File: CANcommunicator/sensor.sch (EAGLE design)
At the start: 19 parts, among them Y1 32.768kHz

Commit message: CAN sensor data ingestion
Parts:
- removed C11, C12: 560pF, SparkFun-Capacitors:560PF-0603-50V-5%
- removed R7: 4.7k, SparkFun-Resistors:4.7KOHM-0603-1/10W-1%
- added ACCEL: 22-23-2051, con-molex:22-23-2051
- added ADC, CAN0: 22-23-2021, con-molex:22-23-2021
- added CC2, CC3: 560pF, SparkFun-Capacitors:560PF-0603-50V-5%
- added CR1: 4.7k, SparkFun-Resistors:4.7KOHM-0603-1/10W-1%
- added IR1: 330, SparkFun-Resistors:330OHM-0603-1/10W-1%
- added PROGRAM: CORTEX_DEBUG_PTH, SparkFun-Connectors:CORTEX_DEBUG_PTH
- added SENSOR: 22-23-2031, con-molex:22-23-2031
- added SERCOM0, SERCOM1: 22-23-2041, con-molex:22-23-2041
- added STATUS: GREEN, SparkFun-LED:LED3MM
- renumbered C1 to PC2, C13 to CC1, C2 to PC1, C3 to IC2, C4 to IC3, C5 to IC1, C6 to OC1, C7 to OC2, R8 to CR3, R9 to CR2, U$1 to MCU, Y1 to O1
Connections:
- net N$1 renamed VDDANA
- net N$2 renamed VDDCORE
- net N$3 renamed XIN32
- net N$5 renamed XOUT32
- removed net 5V: CANI1.VSS, CC1.2
- removed net N$12: CANI1.RS, R7.1
- removed net N$13: C11.1, CR2.1
- removed net N$14: C12.1, CR3.1
- new net A0: ADC-1.S, MCU.PA02(AIN0)
- new net A1: ADC-2.S, MCU.PA03(AIN1)
- new net A4: MCU.PA04(AIN4), SENSOR-2.S
- new net A5: ACCEL-3.S, MCU.PA05(AIN5)
- new net A6: ACCEL-4.S, MCU.PA06(AIN6)
- new net A7: ACCEL-5.S, MCU.PA07(AIN7)
- new net C1HRC: CC2.1, CR2.1
- new net C1LRC: CC3.1, CR3.1
- new net C1RS: CANI1.RS, CR1.1
- new net LEDA: MCU.PA28, STATUS.A
- new net LEDC: IR1.2, STATUS.C
- new net RESET: MCU./RESET, PROGRAM.!RESET
- new net S00: MCU.PA08(SER00), SERCOM0-1.S
- new net S01: MCU.PA09(SER01), SERCOM0-2.S
- new net S02: MCU.PA10(SER02), SERCOM0-3.S
- new net S03: MCU.PA11(SER03), SERCOM0-4.S
- new net S10: MCU.PA16(SER10), SERCOM1-1.S
- new net S11: MCU.PA17(SER11), SERCOM1-2.S
- new net S12: MCU.PA18(SER12), SERCOM1-3.S
- new net S13: MCU.PA19(SER13), SERCOM1-4.S
- new net SWDCLK: MCU.PA30(SWCLK), PROGRAM.SWDCLK/TCK
- new net SWDIO: MCU.PA31(SWDIO), PROGRAM.SWDIO/TMS
- net CAN1H: now also CAN0-1.S
- net CAN1L: now also CAN0-2.S
- net CAN1RX: now also MCU.PA25(CANRX)
- net CAN1TX: now also MCU.PA24(CANTX)
- net GND: now also ACCEL-2.S, CC2.2, CC3.2, CR1.2, IR1.1, PROGRAM.GND@3, PROGRAM.GND@5, PROGRAM.GNDDTCT, SENSOR-3.S; no longer C11.2, C12.2, R7.2
- net VCC: now also ACCEL-1.S, CANI1.VSS, CC1.2, PROGRAM.VCC, SENSOR-1.S
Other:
- note added: "1"
- note added: "CAN Sensor Data Ingestion"
- note added: "EL-05154-AA"
- moved on the sheet: PWR-1, PWR-2

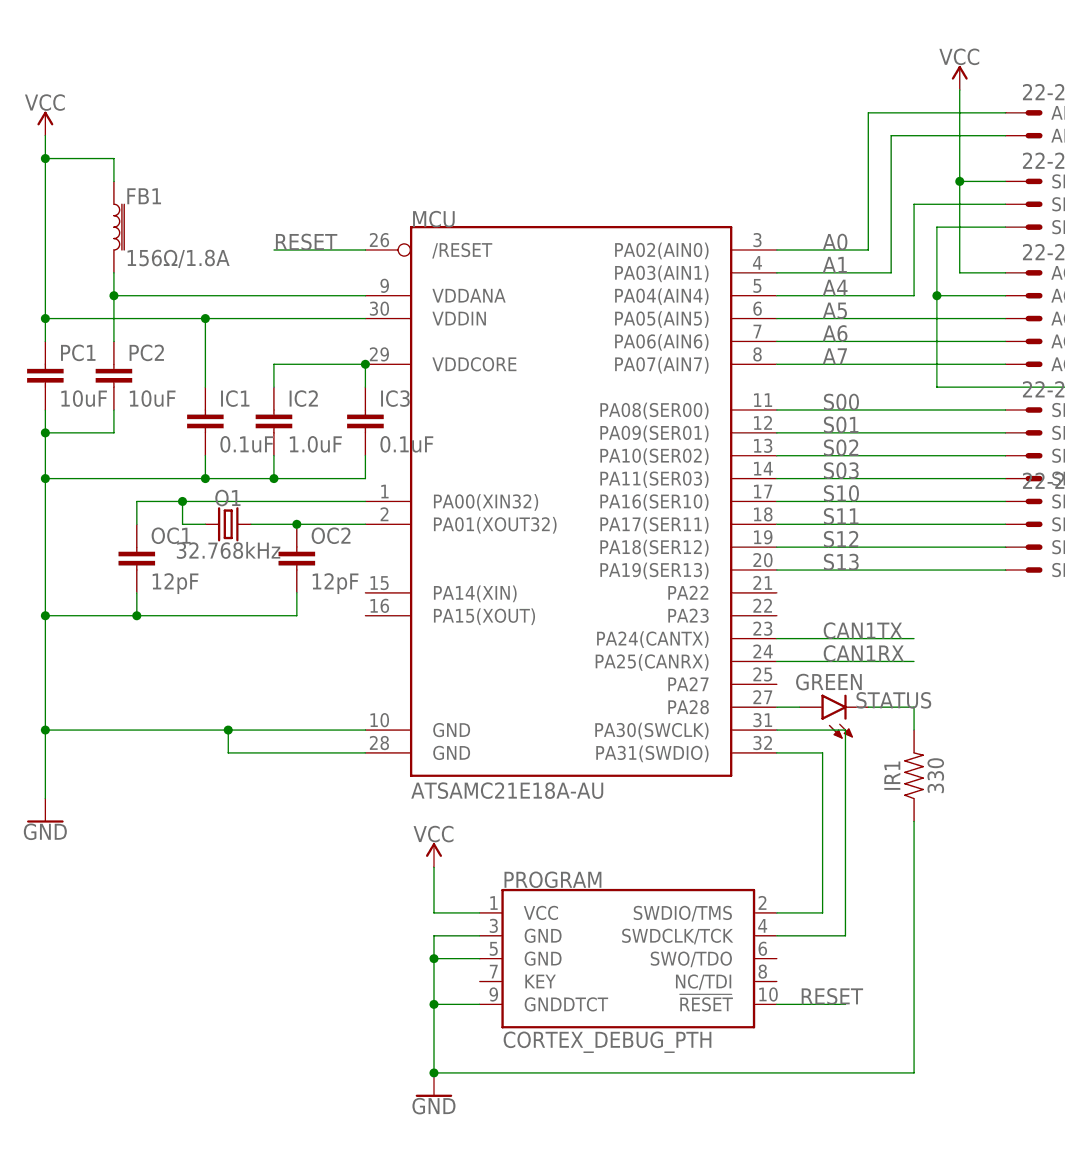
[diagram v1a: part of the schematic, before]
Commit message: Add pullup on SWDCLK and RC filter on RESET_L
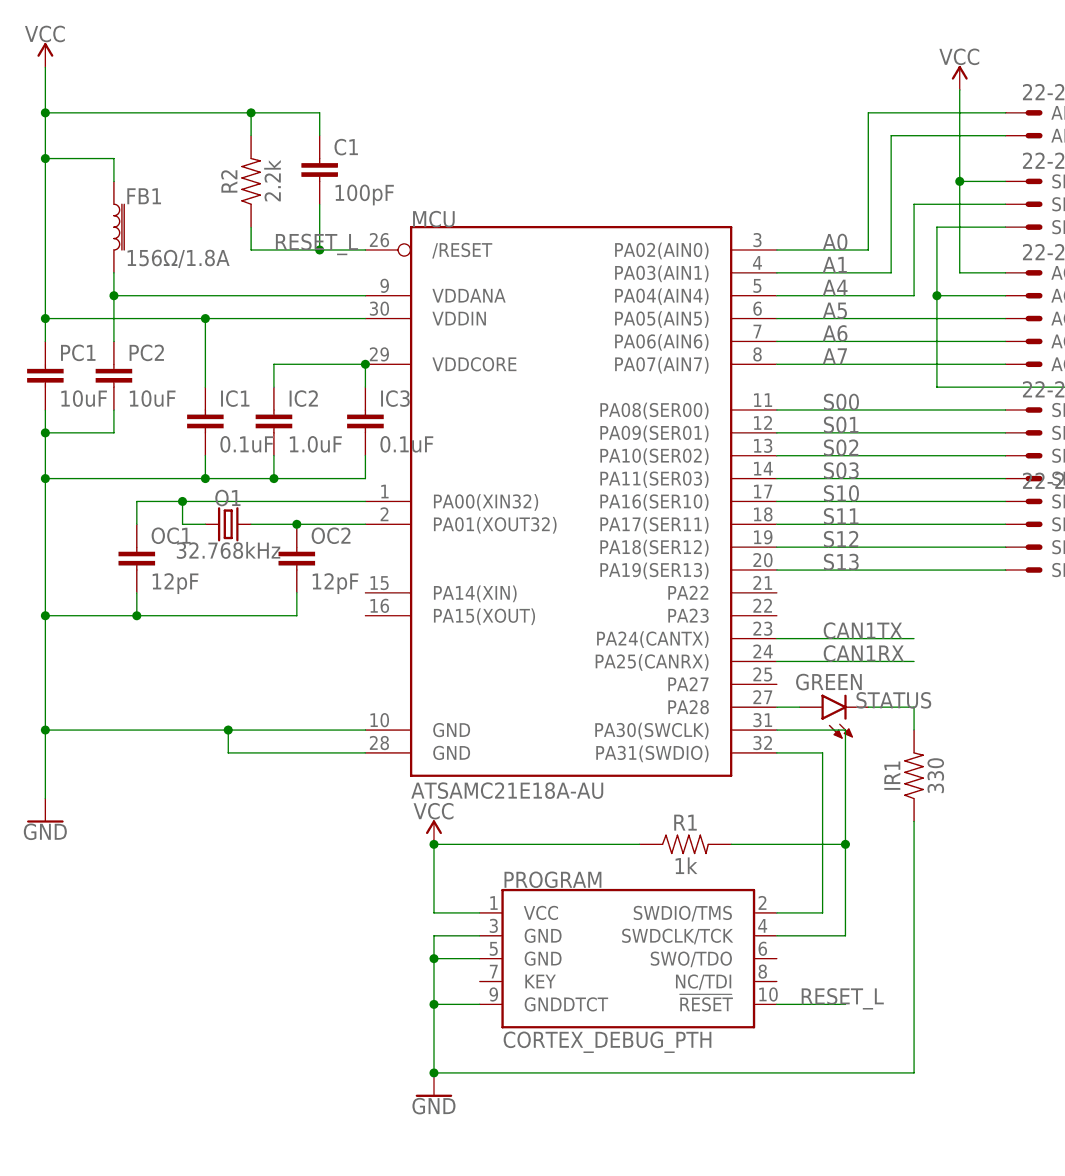
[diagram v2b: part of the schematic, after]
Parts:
- added C1: 100pF, SparkFun-Capacitors:100PF-0603-50V-5%
- added R1: 1k, SparkFun-Resistors:1KOHM-0603-1/10W-1%
- added R2: 2.2k, SparkFun-Resistors:2.2KOHM-0603-1/10W-1%
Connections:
- removed net RESET: MCU./RESET, PROGRAM.!RESET
- new net RESET_L: C1.2, MCU./RESET, PROGRAM.!RESET, R2.1
- net SWDCLK: now also R1.2
- net VCC: now also C1.1, R1.1, R2.2
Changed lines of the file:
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@@
 <part name="SENSOR" library="con-molex" library_urn="urn:adsk.eagle:library:165" deviceset="22-23-2031" device=""/>
 <part name="ADC" library="con-molex" library_urn="urn:adsk.eagle:library:165" deviceset="22-23-2021" device=""/>
+<part name="R1" library="SparkFun-Resistors" library_urn="urn:adsk.eagle:library:532" deviceset="1KOHM" device="-0603-1/10W-1%" package3d_urn="urn:adsk.eagle:package:39650/1" value="1k"/>
+<part name="R2" library="SparkFun-Resistors" library_urn="urn:adsk.eagle:library:532" deviceset="2.2KOHM" device="-0603-1/10W-1%" package3d_urn="urn:adsk.eagle:package:39650/1" value="2.2k"/>
+<part name="C1" library="SparkFun-Capacitors" library_urn="urn:adsk.eagle:library:510" deviceset="100PF" device="-0603-50V-5%" package3d_urn="urn:adsk.eagle:package:37414/1" value="100pF"/>
 </parts>
 <sheets>
@@
 <attribute name="VALUE" x="21.59" y="172.72" size="1.778" layer="96" font="vector" align="top-left"/>
 </instance>
-<instance part="SUPPLY2" gate="G$1" x="12.7" y="185.42">
-<attribute name="VALUE" x="12.7" y="188.214" size="1.778" layer="96" align="bottom-center"/>
+<instance part="SUPPLY2" gate="G$1" x="12.7" y="193.04">
+<attribute name="VALUE" x="12.7" y="195.834" size="1.778" layer="96" align="bottom-center"/>
 </instance>
 <instance part="PC2" gate="G$1" x="20.32" y="157.48">
@@
 <attribute name="VALUE" x="63.5" y="84.074" size="1.778" layer="96" font="vector"/>
 </instance>
-<instance part="SUPPLY3" gate="G$1" x="55.88" y="104.14">
-<attribute name="VALUE" x="55.88" y="106.934" size="1.778" layer="96" align="bottom-center"/>
+<instance part="SUPPLY3" gate="G$1" x="55.88" y="106.68">
+<attribute name="VALUE" x="55.88" y="109.474" size="1.778" layer="96" align="bottom-center"/>
 </instance>
 <instance part="GND3" gate="1" x="55.88" y="78.74">
@@
 <instance part="ADC" gate="-2" x="121.92" y="185.42">
 <attribute name="NAME" x="124.46" y="184.658" size="1.524" layer="95"/>
+</instance>
+<instance part="R1" gate="G$1" x="83.82" y="106.68">
+<attribute name="NAME" x="83.82" y="108.204" size="1.778" layer="95" font="vector" align="bottom-center"/>
+<attribute name="VALUE" x="83.82" y="105.156" size="1.778" layer="96" font="vector" align="top-center"/>
+</instance>
+<instance part="R2" gate="G$1" x="35.56" y="180.34" rot="R90">
+<attribute name="NAME" x="34.036" y="180.34" size="1.778" layer="95" font="vector" rot="R90" align="bottom-center"/>
+<attribute name="VALUE" x="37.084" y="180.34" size="1.778" layer="96" font="vector" rot="R90" align="top-center"/>
+</instance>
+<instance part="C1" gate="G$1" x="43.18" y="180.34">
+<attribute name="NAME" x="44.704" y="183.261" size="1.778" layer="95" font="vector"/>
+<attribute name="VALUE" x="44.704" y="178.181" size="1.778" layer="96" font="vector"/>
 </instance>
 </instances>
@@
 <pinref part="SUPPLY2" gate="G$1" pin="VCC"/>
 <pinref part="MCU" gate="G$1" pin="VDDIN"/>
-<wire x1="12.7" y1="185.42" x2="12.7" y2="182.88" width="0.1524" layer="91"/>
+<wire x1="12.7" y1="193.04" x2="12.7" y2="187.96" width="0.1524" layer="91"/>
+<wire x1="12.7" y1="187.96" x2="12.7" y2="182.88" width="0.1524" layer="91"/>
 <wire x1="12.7" y1="182.88" x2="12.7" y2="165.1" width="0.1524" layer="91"/>
 <wire x1="12.7" y1="165.1" x2="30.48" y2="165.1" width="0.1524" layer="91"/>
@@
 <wire x1="30.48" y1="157.48" x2="30.48" y2="165.1" width="0.1524" layer="91"/>
 <junction x="30.48" y="165.1"/>
+<pinref part="R2" gate="G$1" pin="2"/>
+<wire x1="35.56" y1="185.42" x2="35.56" y2="187.96" width="0.1524" layer="91"/>
+<wire x1="35.56" y1="187.96" x2="12.7" y2="187.96" width="0.1524" layer="91"/>
+<junction x="12.7" y="187.96"/>
+<wire x1="35.56" y1="187.96" x2="43.18" y2="187.96" width="0.1524" layer="91"/>
+<junction x="35.56" y="187.96"/>
+<pinref part="C1" gate="G$1" pin="1"/>
+<wire x1="43.18" y1="187.96" x2="43.18" y2="185.42" width="0.1524" layer="91"/>
 </segment>
 <segment>
 <pinref part="SUPPLY3" gate="G$1" pin="VCC"/>
 <pinref part="PROGRAM" gate="G$1" pin="VCC"/>
-<wire x1="55.88" y1="104.14" x2="55.88" y2="99.06" width="0.1524" layer="91"/>
+<wire x1="55.88" y1="106.68" x2="55.88" y2="99.06" width="0.1524" layer="91"/>
 <wire x1="55.88" y1="99.06" x2="60.96" y2="99.06" width="0.1524" layer="91"/>
+<pinref part="R1" gate="G$1" pin="1"/>
+<wire x1="78.74" y1="106.68" x2="55.88" y2="106.68" width="0.1524" layer="91"/>
+<junction x="55.88" y="106.68"/>
 </segment>
 <segment>
@@
 <wire x1="93.98" y1="119.38" x2="101.6" y2="119.38" width="0.1524" layer="91"/>
 <pinref part="PROGRAM" gate="G$1" pin="SWDCLK/TCK"/>
-<wire x1="101.6" y1="119.38" x2="101.6" y2="96.52" width="0.1524" layer="91"/>
+<wire x1="101.6" y1="119.38" x2="101.6" y2="106.68" width="0.1524" layer="91"/>
+<wire x1="101.6" y1="106.68" x2="101.6" y2="96.52" width="0.1524" layer="91"/>
 <wire x1="101.6" y1="96.52" x2="93.98" y2="96.52" width="0.1524" layer="91"/>
-</segment>
-</net>
-<net name="RESET" class="0">
+<pinref part="R1" gate="G$1" pin="2"/>
+<wire x1="88.9" y1="106.68" x2="101.6" y2="106.68" width="0.1524" layer="91"/>
+<junction x="101.6" y="106.68"/>
+</segment>
+</net>
+<net name="RESET_L" class="0">
 <segment>
 <pinref part="MCU" gate="G$1" pin="/RESET"/>
-<wire x1="48.26" y1="172.72" x2="38.1" y2="172.72" width="0.1524" layer="91"/>
+<wire x1="48.26" y1="172.72" x2="43.18" y2="172.72" width="0.1524" layer="91"/>
 <label x="38.1" y="172.72" size="1.778" layer="95"/>
-</segment>
-<segment>
+<pinref part="R2" gate="G$1" pin="1"/>
+<wire x1="43.18" y1="172.72" x2="35.56" y2="172.72" width="0.1524" layer="91"/>
+<wire x1="35.56" y1="175.26" x2="35.56" y2="172.72" width="0.1524" layer="91"/>
+<pinref part="C1" gate="G$1" pin="2"/>
+<wire x1="43.18" y1="177.8" x2="43.18" y2="172.72" width="0.1524" layer="91"/>
+<junction x="43.18" y="172.72"/>
+</segment>
+<segment>

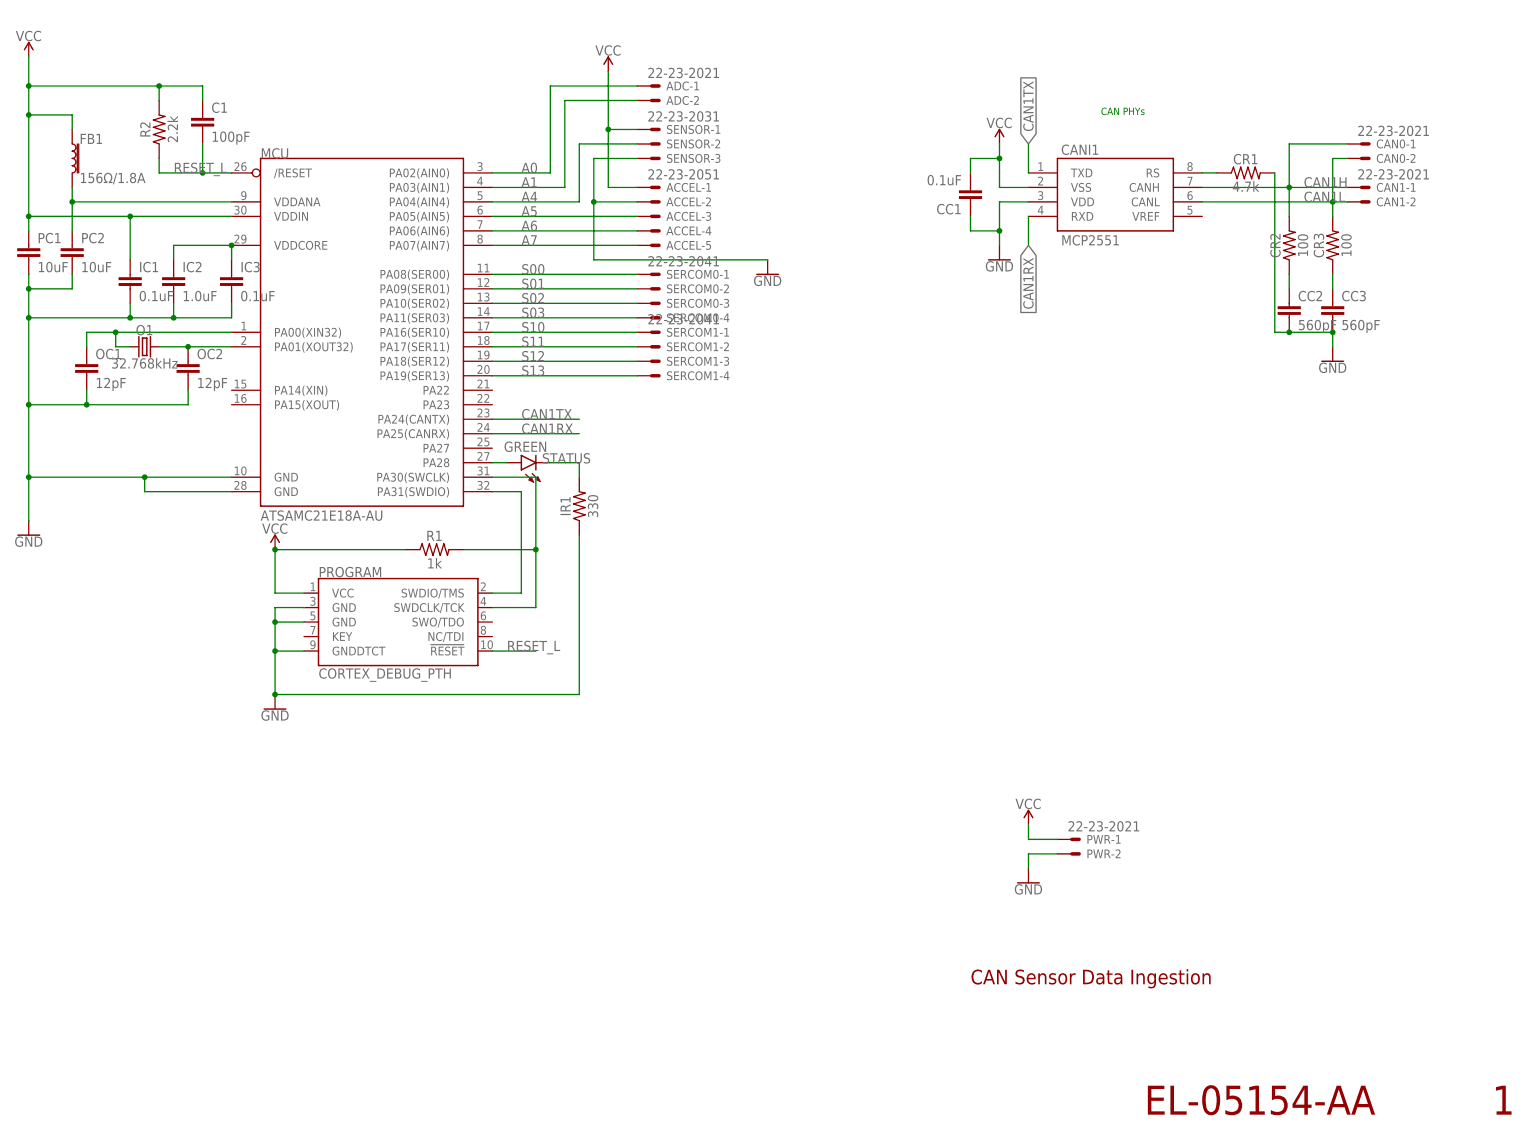
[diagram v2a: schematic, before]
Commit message: Move some signal traces away from capacitors
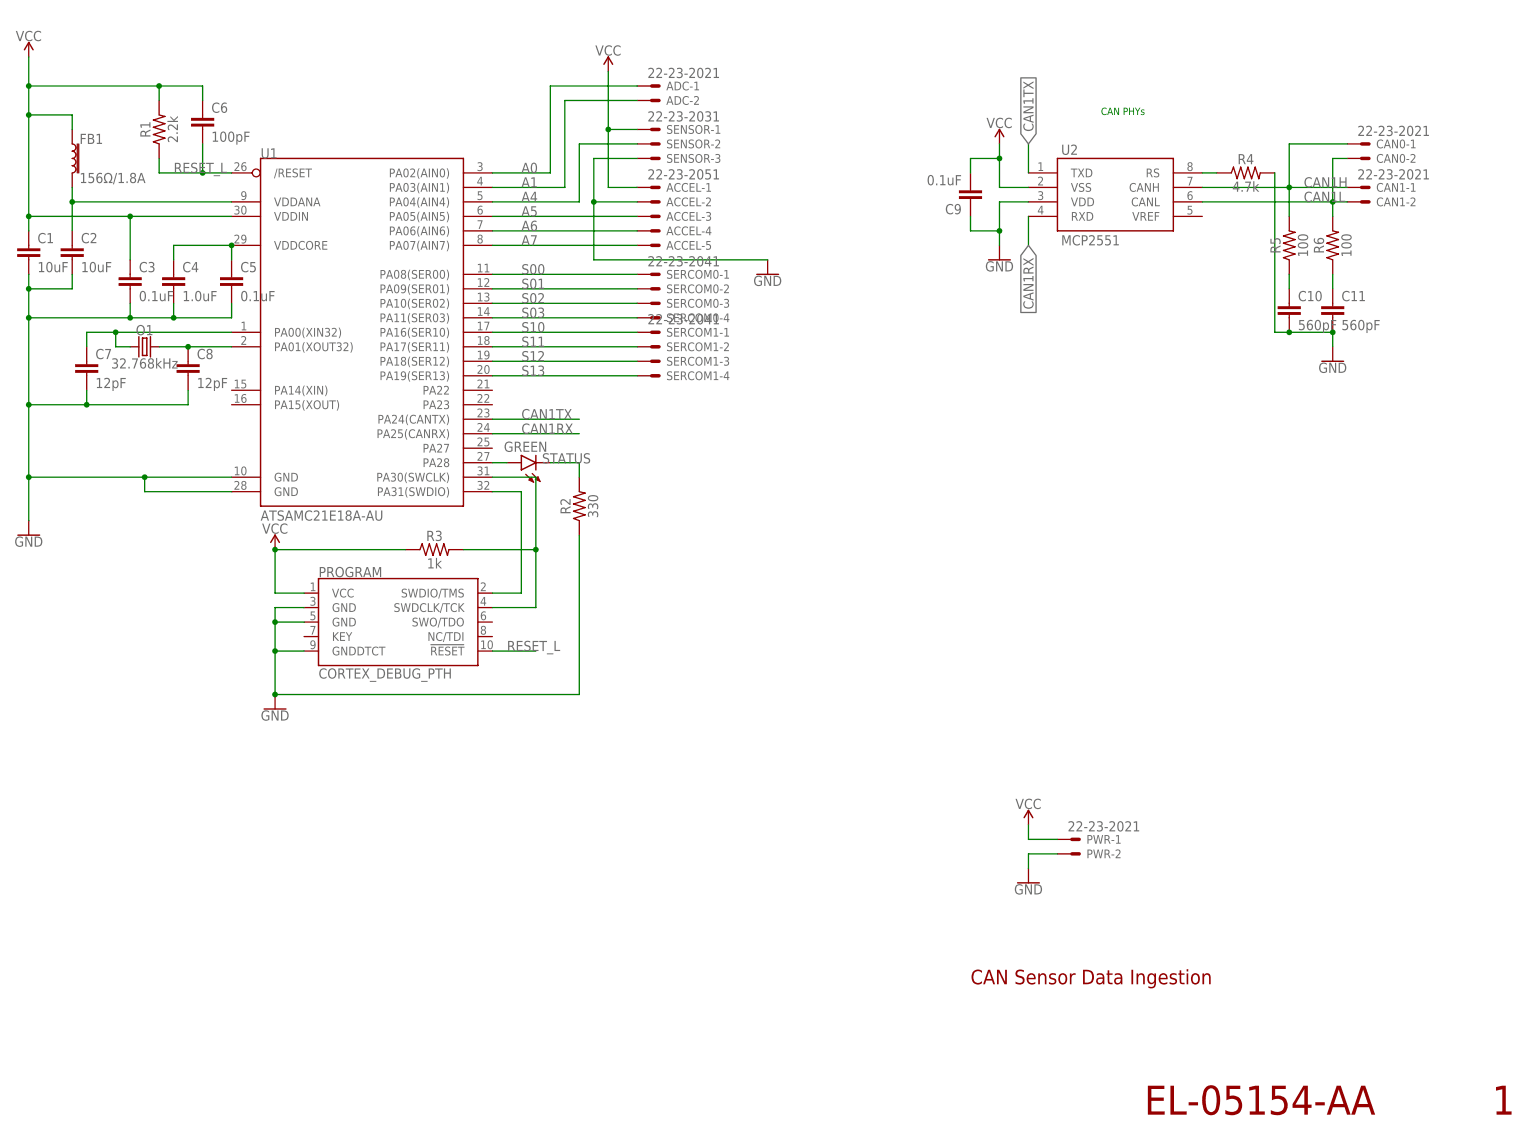
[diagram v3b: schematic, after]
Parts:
- removed IR1: 330, SparkFun-Resistors:330OHM-0603-1/10W-1%
- removed PC1: 10uF, SparkFun-Capacitors:10UF-0603-6.3V-20%
- added C6: 100pF, SparkFun-Capacitors:100PF-0603-50V-5%
- added R3: 1k, SparkFun-Resistors:1KOHM-0603-1/10W-1%
- C1: value 100pF -> 10uF; device SparkFun-Capacitors:100PF-0603-50V-5% -> SparkFun-Capacitors:10UF-0603-6.3V-20%
- R1: value 1k -> 2.2k; device SparkFun-Resistors:1KOHM-0603-1/10W-1% -> SparkFun-Resistors:2.2KOHM-0603-1/10W-1%
- R2: value 2.2k -> 330; device SparkFun-Resistors:2.2KOHM-0603-1/10W-1% -> SparkFun-Resistors:330OHM-0603-1/10W-1%
- renumbered CANI1 to U2, CC1 to C9, CC2 to C10, CC3 to C11, CR1 to R4, CR2 to R5, CR3 to R6, IC1 to C3, IC2 to C4, IC3 to C5, MCU to U1, OC1 to C7, OC2 to C8, PC2 to C2
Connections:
- net GND: now also C1.2, R2.1; no longer IR1.1, PC1.2
- net LEDC: now also R2.2; no longer IR1.2
- net RESET_L: now also C6.2, R1.1; no longer C1.2, R2.1
- net SWDCLK: now also R3.2; no longer R1.2
- net VCC: now also C6.1, R1.2, R3.1; no longer PC1.1, R1.1, R2.2
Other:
- moved on the sheet: C1, R1, R2
